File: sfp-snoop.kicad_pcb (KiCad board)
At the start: 2 copper layers, 22.9 x 53.3 mm, 29 parts, among them J1 SFP+, J2 Conn_01x20, J3 Conn_01x20, U1 AIC1221-33GY3TR, U2 AP2191WG-7

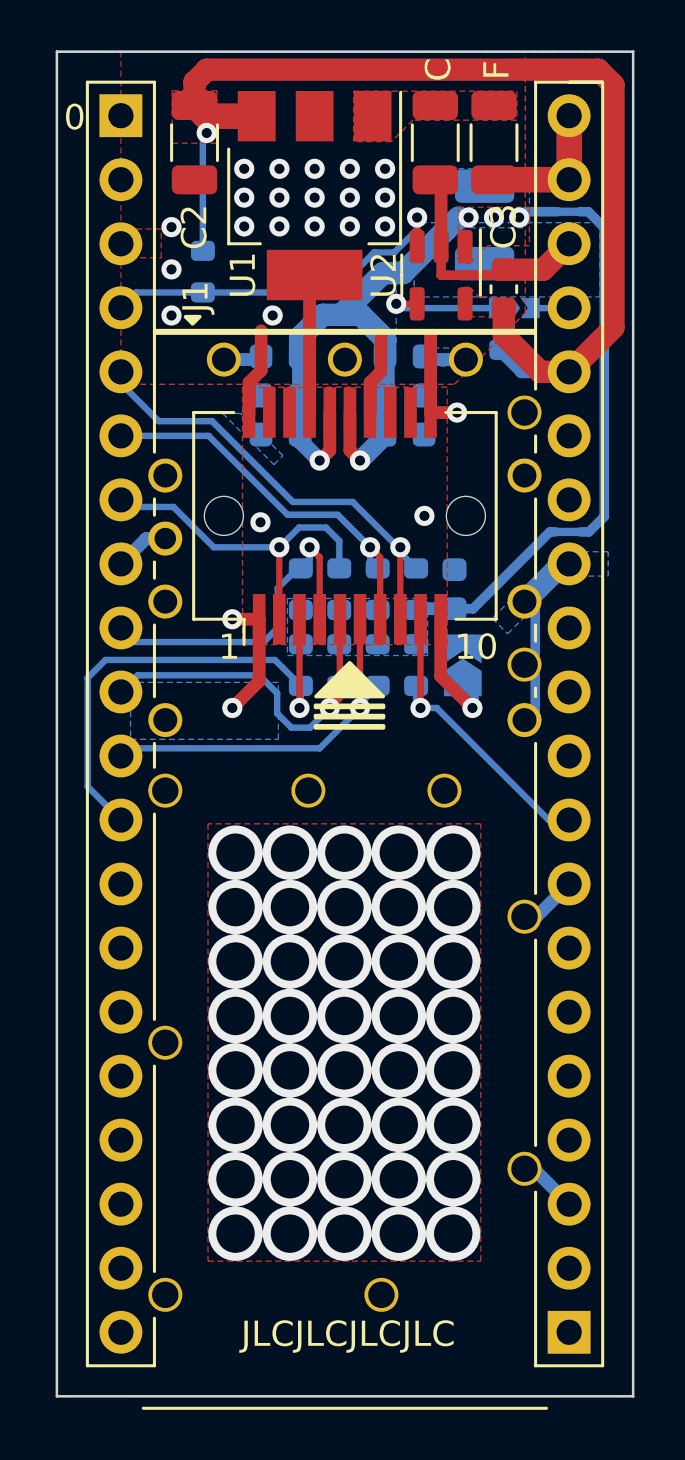
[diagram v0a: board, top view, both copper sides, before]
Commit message: Update Nokia G-010S-A pinout
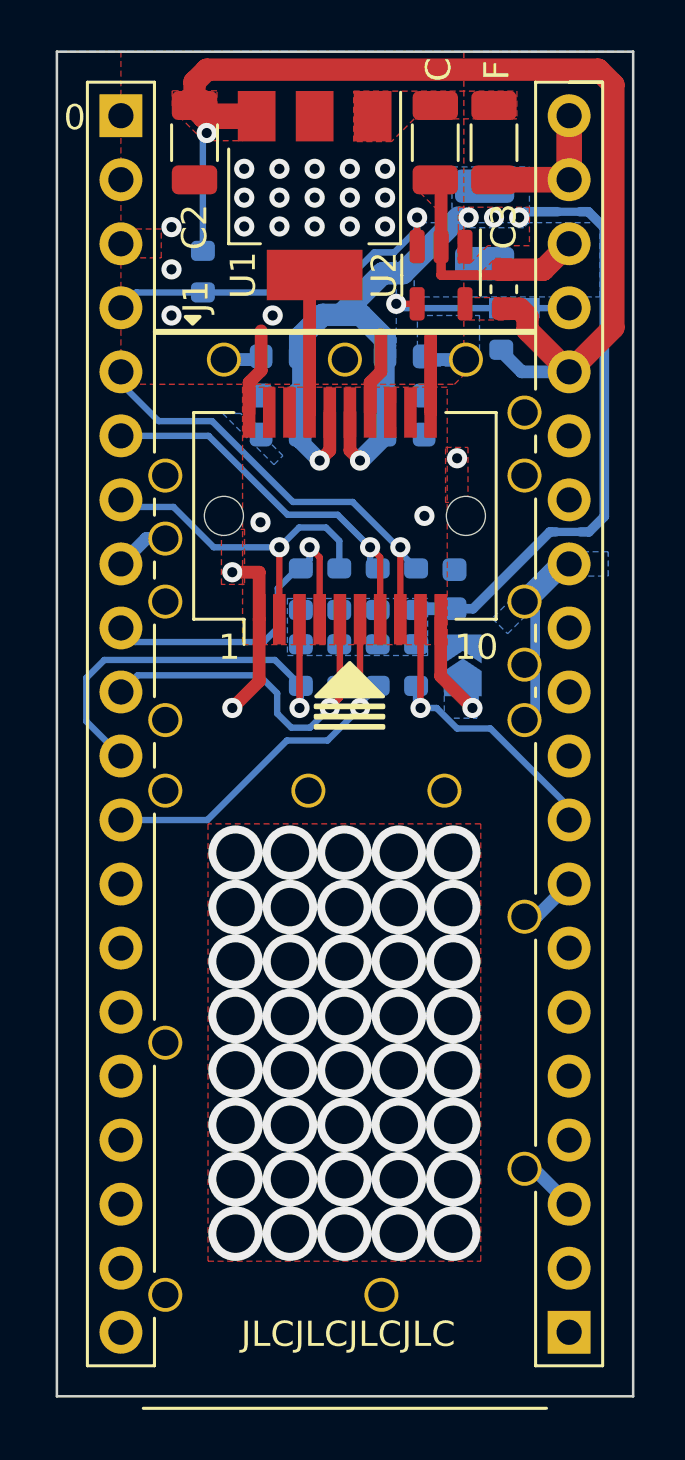
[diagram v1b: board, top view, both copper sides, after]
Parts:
- removed REF**: OSHW-Logo_5.7x6mm_SilkScreen, Symbol:OSHW-Logo_5.7x6mm_SilkScreen
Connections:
- J1 pad 3: /GPIO9 -> /GPIO8
- J1 pad 6: /GPIO8 -> /GPIO9
- R3 pad 1: /GPIO9 -> /GPIO8
- R6 pad 1: /GPIO8 -> /GPIO9
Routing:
- net /GPIO9: track 19.8 -> 16.0 mm
- net /GPIO8: track 15.0 -> 17.3 mm
- added copper zone on B.Cu, net Net-(J1-VeeRX)
